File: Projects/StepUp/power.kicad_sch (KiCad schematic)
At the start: 45 parts, among them J5 Conn_01x02, J6 Conn_01x02, J7 Conn_01x02, J8 Conn_01x02, Q3 BSS83P, Q4 BSS83P, U5 MCP73832T-2ACI_OT, U6 NCP1117-3.3_SOT223, U7 MIC2253

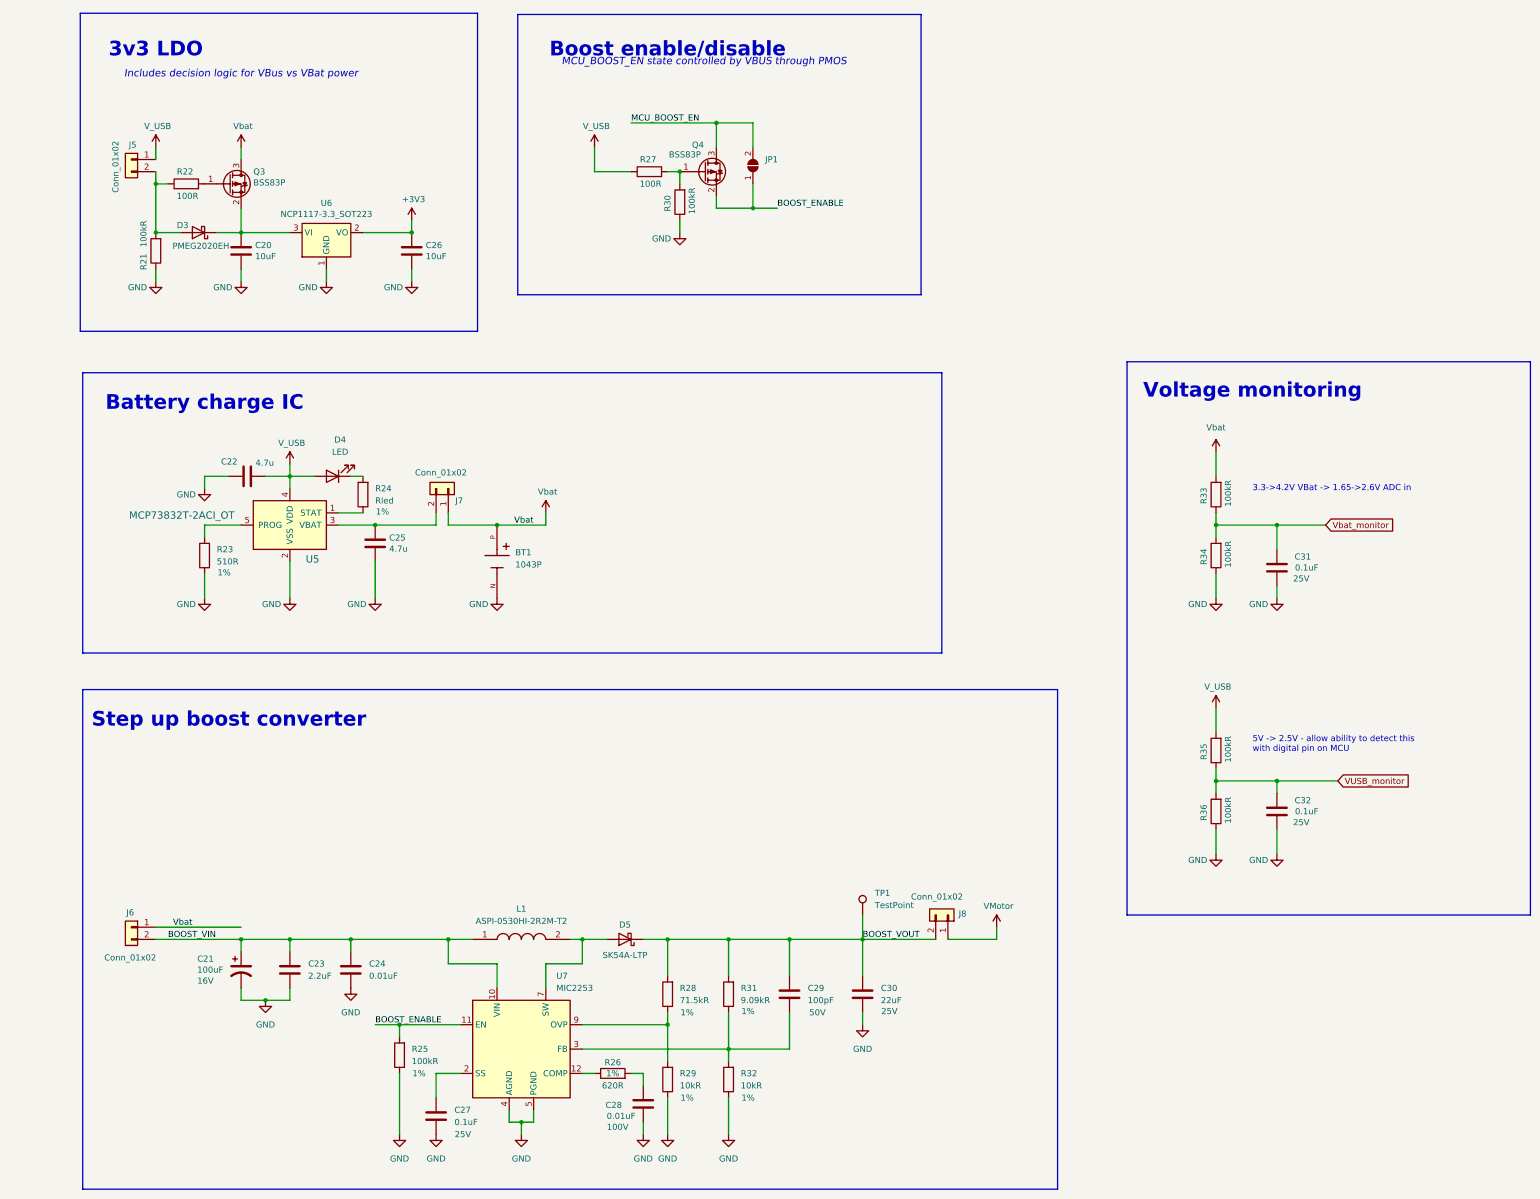
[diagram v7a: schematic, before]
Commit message: feat(schematic): Ready for layout
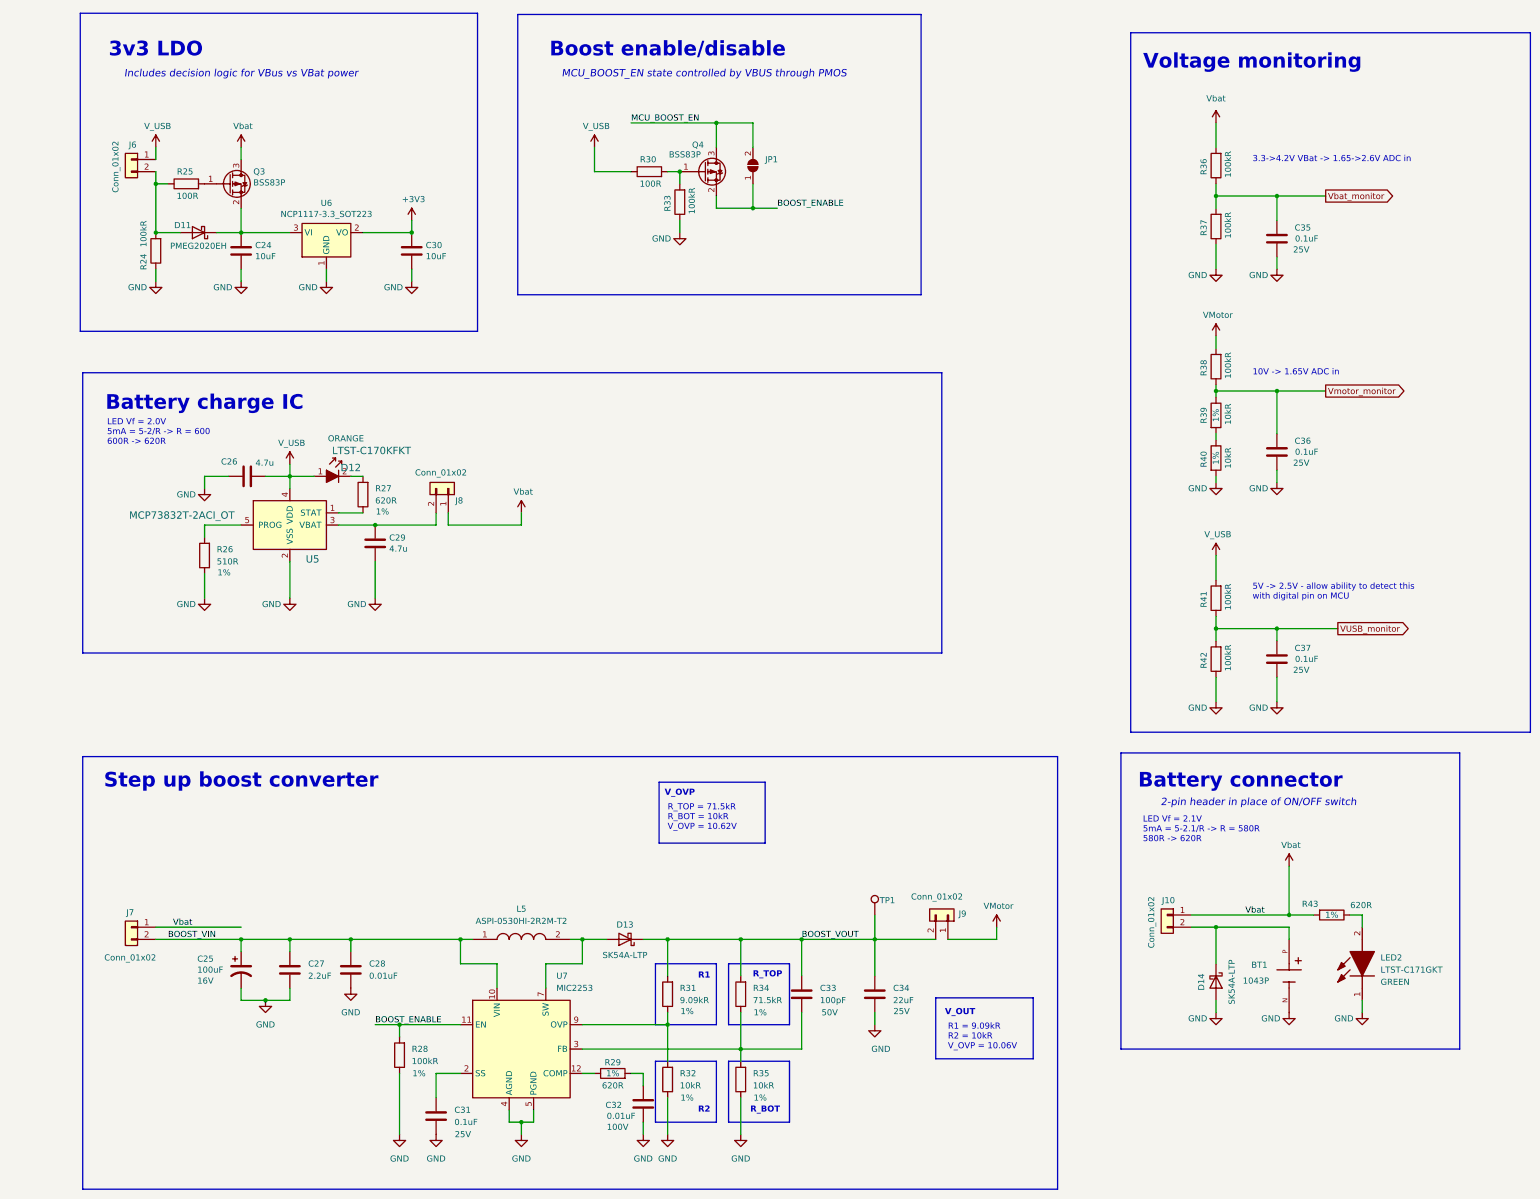
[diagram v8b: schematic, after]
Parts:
- removed D4: LED, LED_SMD:LED_0805_2012Metric, symbol Device:LED
- removed R28: 71.5kR, Resistor_SMD:R_0603_1608Metric, symbol Device:R
- added C36: 0.1uF, Capacitor_SMD:C_0603_1608Metric, symbol Device:C
- added D12: LTST-C170KFKT, digikey-footprints:0805, symbol dk_LED-Indication-Discrete:LTST-C170KFKT
- added D14: SK54A-LTP, Diode_SMD:D_SMA, symbol Device:D_Schottky
- added J10: Conn_01x02, Connector_PinHeader_2.54mm:PinHeader_1x02_P2.54mm_Vertical, symbol Connector_Generic:Conn_01x02
- added LED2: LTST-C171GKT, Samacsys:LEDC2012X90N, symbol Samacsys:LTST-C171GKT
- added R34: 71.5kR, Resistor_SMD:R_0603_1608Metric, symbol Device:R
- added R38: 100kR, Resistor_SMD:R_0603_1608Metric, symbol Device:R
- added R39, R40: 10kR, Resistor_SMD:R_0603_1608Metric, symbol Device:R
- added R43: 620R, Resistor_SMD:R_0603_1608Metric, symbol Device:R
- R27: renamed from R24; value Rled -> 620R
- renumbered C20 to C24, C21 to C25, C22 to C26, C23 to C27, C24 to C28, C25 to C29, C26 to C30, C27 to C31, C28 to C32, C29 to C33, C30 to C34, C31 to C35, C32 to C37, D3 to D11, D5 to D13, J5 to J6, J6 to J7, J7 to J8, J8 to J9, L1 to L5, R21 to R24, R22 to R25, R23 to R26, R25 to R28, R26 to R29, R27 to R30, R29 to R32, R30 to R33, R32 to R35, R33 to R36, R34 to R37, R35 to R41, R36 to R42
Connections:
- net BOOST_VOUT: now also R34.2
- net GND: now also C36.1, D14.2 (A), LED2.1 (K), R40.2
- net VMotor: now also R38.2
- net V_USB: now also D12.1
- net Vbat: now also J10.1 (Pin_1), R43.2; no longer BT1.P
- net at C33.2, R35.2, U7.3 (FB): now also R34.1; no longer R31.1
- net at R32.2, U7.9 (OVP): now also R31.1
- net at R27.2: now also D12.2
- new net: LED2.2 (A), R43.1
- new net: BT1.P, D14.1 (K), J10.2 (Pin_2)
- new net: R39.2, R40.1
- new net Vmotor_monitor: C36.2, R38.1, R39.1
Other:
- note added: "10V -> 1.65V ADC in"
- note added: "2-pin header in place of ON/OFF switch"
- note added: "Battery connector"
- note added: "LED Vf = 2.0V 5mA = 5-2/R -> R = 600 600R -> 620R"
- note added: "LED Vf = 2.1V 5mA = 5-2.1/R -> R = 580R 580R -> 620R"
- note added: "R1"
- note added: "R1 = 9.09kR R2 = 10kR V_OVP = 10.06V"
- note added: "R2"
- note added: "R_BOT"
- note added: "R_TOP"
- note added: "R_TOP = 71.5kR R_BOT = 10kR V_OVP = 10.62V"
- note added: "V_OUT"
- note added: "V_OVP"
- title: (none) -> Power
- moved on the sheet: C33, C34, C35, C37, R35, R36, R37, R41, R42, TP1
